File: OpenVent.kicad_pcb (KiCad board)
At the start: 2 copper layers, 195.5 x 61 mm, 217 parts, among them CN1 2x10_Way_2.54mm_Pitch_Header, J1 OpenVent_Barrel_Connector, Q1 DMMT5401-7-F, Q12 2N7002BK, Q13 2N7002BK, Q14 AOD4185, Q2 AOD4185, Q3 AOD4185, Q4 DMMT5401-7-F, Q5 2N7002BK, Q6 2N7002BK, Q7 2N7002BK, Q8 SSM3K341R, Q9 2N7002BK, U1 TMP236A4DBZT, U10 MPXV4006GP, U11 MPXV4006DP, U12 TLV2333IDR, U13 TLV7042DGKR, U14 LT3796, U15 FT2232HL-REEL, U16 TLV2333IDR, U2 STM32L412R8T6, U3 TI_TXB0108PWR, U4 BD50FC0WEFJ-E2, U5 LDL212D33R, U6 LDL212D33R, U7 LMC6772AIMX, U8 VNH5019ATR-E, U9 LDL212D33R, X1 ABM3B-16.000MHZ, X2 ABM3B-12.000MHZ

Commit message: Update OpenVent.kicad_pcb
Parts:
- JP2: moved to B.Cu
- moved JP2 50.9 mm to (142.7, 123.2), turned to 270 degrees
- moved C10 25.0 mm to (75.0, 124.4)
- moved C7 25.0 mm to (71.0, 124.4)
- moved D1 25.0 mm to (53.5, 126.9)
- moved TVS1 25.0 mm to (67.1, 125.1)
- moved C4 25.0 mm to (71.0, 126.9)
- moved FL1 25.0 mm to (74.8, 126.9)
- moved RV1 25.0 mm to (61.8, 125.9)
- moved C15 13.0 mm to (226.3, 109.4)
- moved C16 13.0 mm to (229.8, 98.6)
- moved C40 13.0 mm to (167.1, 104.1)
- moved C41 13.0 mm to (174.1, 96.8)
- moved C53 13.0 mm to (159.1, 105.2)
- moved D3 13.0 mm to (71.8, 87.2)
- moved D4 13.0 mm to (67.8, 87.2)
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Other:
- board size 195.5 x 61 mm -> 195.5 x 76.2 mm

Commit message: Mounting holes x4 have been added to the PCB
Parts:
- added C110: 1uF_0603_Ceramic_Capacitor,_10%,_50V,_X5R, Capacitor_SMD:C_0603_1608Metric, F.Cu at (400.1, 24.1)
- added C117: 1uF_0603_Ceramic_Capacitor,_10%,_50V,_X5R, Capacitor_SMD:C_0603_1608Metric, F.Cu at (396.1, 26.6)
- added C13: 1uF_0603_Ceramic_Capacitor,_10%,_50V,_X5R, Capacitor_SMD:C_0603_1608Metric, F.Cu at (415.3, 33.0)
- added C22: 10nF_0603_Ceramic_Capacitor,_10%,_50V,_X7R-, Capacitor_SMD:C_0603_1608Metric, F.Cu at (374.1, 15.8)
- added C62: 10uF_0805_Ceramic_Capacitor_10%_X7R_10V, Capacitor_SMD:C_0805_2012Metric, F.Cu at (365.5, 21.8)
- added C63: 10uF_0805_Ceramic_Capacitor_10%_X7R_10V, Capacitor_SMD:C_0805_2012Metric, F.Cu at (361.0, 21.8)
- added C64: 470pF_0603_Ceramic_Capacitor,_5%,_100V,_C0G, Capacitor_SMD:C_0603_1608Metric, F.Cu at (374.4, 13.3)
- added C65: 10uF_0805_Ceramic_Capacitor_10%_X7R_10V, Capacitor_SMD:C_0805_2012Metric, F.Cu at (356.6, 21.8)
- added C66: 100nF_0603_Ceramic_Capacitor,_10%,_X7R,_25V, Capacitor_SMD:C_0603_1608Metric, F.Cu at (375.7, 10.8)
- added C67: 10nF_0603_Ceramic_Capacitor,_10%,_50V,_X7R-, Capacitor_SMD:C_0603_1608Metric, F.Cu at (370.1, 15.8)
- added C68: 1uF_0603_Ceramic_Capacitor,_10%,_50V,_X5R, Capacitor_SMD:C_0603_1608Metric, F.Cu at (375.7, 8.25)
- added C69: 470pF_0603_Ceramic_Capacitor,_5%,_100V,_C0G, Capacitor_SMD:C_0603_1608Metric, F.Cu at (370.4, 13.3)
- added C70: 10nF_0603_Ceramic_Capacitor,_10%,_50V,_X7R-, Capacitor_SMD:C_0603_1608Metric, F.Cu at (371.7, 10.8)
- added C71: 470pF_0603_Ceramic_Capacitor,_5%,_100V,_C0G, Capacitor_SMD:C_0603_1608Metric, F.Cu at (376.3, 3.23)
- added C72: 1uF_0603_Ceramic_Capacitor,_10%,_50V,_X5R, Capacitor_SMD:C_0603_1608Metric, F.Cu at (371.7, 8.25)
- added C73: 1uF_0603_Ceramic_Capacitor,_10%,_50V,_X5R, Capacitor_SMD:C_0603_1608Metric, F.Cu at (376.3, 5.74)
- added C74: C_1206_47nF_16V_2%_PPS_film, Capacitor_SMD:C_1206_3216Metric, F.Cu at (358.2, 7.84)
- added C75: C_1206_47nF_16V_2%_PPS_film, Capacitor_SMD:C_1206_3216Metric, F.Cu at (352.5, 15.0)
- added C76: C_1206_47nF_16V_2%_PPS_film, Capacitor_SMD:C_1206_3216Metric, F.Cu at (362.8, 1.14)
- added C77: C_1206_47nF_16V_2%_PPS_film, Capacitor_SMD:C_1206_3216Metric, F.Cu at (352.5, 11.6)
- added C78: C_1206_47nF_16V_2%_PPS_film, Capacitor_SMD:C_1206_3216Metric, F.Cu at (357.1, 1.14)
- added C79: C_1206_47nF_16V_2%_PPS_film, Capacitor_SMD:C_1206_3216Metric, F.Cu at (357.1, 4.49)
- added C80: C_1206_47nF_16V_2%_PPS_film, Capacitor_SMD:C_1206_3216Metric, F.Cu at (352.5, 8.29)
- added C81: C_1206_47nF_16V_2%_PPS_film, Capacitor_SMD:C_1206_3216Metric, F.Cu at (362.8, 4.49)
- added C82: C_1206_47nF_16V_2%_PPS_film, Capacitor_SMD:C_1206_3216Metric, F.Cu at (358.2, 11.2)
- added C93: 22uF_1206_Ceramic_Capacitor,_10%,_10V,_X7R, Resistor_SMD:R_1206_3216Metric, F.Cu at (417.3, 23.6)
- added C94: 22uF_1206_Ceramic_Capacitor,_10%,_10V,_X7R, Resistor_SMD:R_1206_3216Metric, F.Cu at (417.3, 20.3)
- added D19: LED_GREEN_0603_SMD, LED_SMD:LED_0603_1608Metric, F.Cu at (385.6, 29.3)
- added J2: Conn_01x02, Connector_PinSocket_2.54mm:PinSocket_1x02_P2.54mm_Vertical, F.Cu at (352.0, 1.79)
- added J3: Conn_01x02, Connector_PinSocket_2.54mm:PinSocket_1x02_P2.54mm_Vertical, F.Cu at (412.2, 21.0)
- added J4: Conn_01x02, Connector_PinSocket_2.54mm:PinSocket_1x02_P2.54mm_Vertical, F.Cu at (407.6, 21.0)
- added JP2: Pin_Header,_1x5-Way,_2.54mm_Pitch, Connector_PinHeader_2.54mm:PinHeader_1x05_P2.54mm_Vertical, F.Cu at (386.7, 1.79)
- added JP5: Pin_Header,_1x6-Way,_2.54mm_Pitch, Connector_PinHeader_2.54mm:PinHeader_1x06_P2.54mm_Vertical, F.Cu at (352.0, 22.6)
- added R10: 100K_0603_Chip_Resistor,_1%,_0.1W, Resistor_SMD:R_0603_1608Metric, F.Cu at (407.3, 33.0)
- added R113: 0R1_0603_Chip_Resistor,_1%,_0.1W, Resistor_SMD:R_0603_1608Metric, F.Cu at (396.1, 21.6)
- added R119: 10k_0603_Chip_Resistor,_1%,_0.1W, Resistor_SMD:R_0603_1608Metric, F.Cu at (389.7, 29.3)
- added R120: 10k_0603_Chip_Resistor,_1%,_0.1W, Resistor_SMD:R_0603_1608Metric, F.Cu at (396.1, 24.1)
- added R122: 0R1_0603_Chip_Resistor,_1%,_0.1W, Resistor_SMD:R_0603_1608Metric, F.Cu at (400.1, 21.6)
- added R124: 10k_0603_Chip_Resistor,_1%,_0.1W, Resistor_SMD:R_0603_1608Metric, F.Cu at (393.7, 29.3)
- added R19: 2k4_0603_Chip_Resistor,_1%,_0.1W, Resistor_SMD:R_0603_1608Metric, F.Cu at (356.4, 24.6)
- added R20: 2k4_0603_Chip_Resistor,_1%,_0.1W, Resistor_SMD:R_0603_1608Metric, F.Cu at (360.4, 24.6)
- added R27: 18k_0603_Chip_Resistor,_1%,_0.1W, Resistor_SMD:R_0603_1608Metric, F.Cu at (366.1, 15.8)
- added R39: R_0603_47K_0.1%_0.1W_Film, Resistor_SMD:R_0603_1608Metric_Pad0.98x0.95mm_HandSolder, F.Cu at (367.8, 3.23)
- added R42: R_0603_47K_0.1%_0.1W_Film, Resistor_SMD:R_0603_1608Metric_Pad0.98x0.95mm_HandSolder, F.Cu at (372.1, 3.23)
- added R43: R_0603_47K_0.1%_0.1W_Film, Resistor_SMD:R_0603_1608Metric_Pad0.98x0.95mm_HandSolder, F.Cu at (367.8, 0.72)
- added R49: R_0603_47K_0.1%_0.1W_Film, Resistor_SMD:R_0603_1608Metric_Pad0.98x0.95mm_HandSolder, F.Cu at (363.2, 7.42)
- added R50: R_0603_47K_0.1%_0.1W_Film, Resistor_SMD:R_0603_1608Metric_Pad0.98x0.95mm_HandSolder, F.Cu at (367.5, 8.25)
- added R53: R_0603_47K_0.1%_0.1W_Film, Resistor_SMD:R_0603_1608Metric_Pad0.98x0.95mm_HandSolder, F.Cu at (376.5, 0.72)
- added R54: R_0603_47K_0.1%_0.1W_Film, Resistor_SMD:R_0603_1608Metric_Pad0.98x0.95mm_HandSolder, F.Cu at (372.1, 5.74)
- added R55: R_0603_47K_0.1%_0.1W_Film, Resistor_SMD:R_0603_1608Metric_Pad0.98x0.95mm_HandSolder, F.Cu at (367.5, 10.8)
- added R56: R_0603_47K_0.1%_0.1W_Film, Resistor_SMD:R_0603_1608Metric_Pad0.98x0.95mm_HandSolder, F.Cu at (361.9, 14.1)
- added R57: R_0603_47K_0.1%_0.1W_Film, Resistor_SMD:R_0603_1608Metric_Pad0.98x0.95mm_HandSolder, F.Cu at (366.2, 13.3)
- added R58: R_0603_47K_0.1%_0.1W_Film, Resistor_SMD:R_0603_1608Metric_Pad0.98x0.95mm_HandSolder, F.Cu at (372.1, 0.72)
- added R59: R_0603_47K_0.1%_0.1W_Film, Resistor_SMD:R_0603_1608Metric_Pad0.98x0.95mm_HandSolder, F.Cu at (367.8, 5.74)
- added R6: 10k_0603_Chip_Resistor,_1%,_0.1W, Resistor_SMD:R_0603_1608Metric, F.Cu at (411.3, 35.5)
- added R60: R_0603_47K_0.1%_0.1W_Film, Resistor_SMD:R_0603_1608Metric_Pad0.98x0.95mm_HandSolder, F.Cu at (363.2, 9.93)
- added R61: R_0603_47K_0.1%_0.1W_Film, Resistor_SMD:R_0603_1608Metric_Pad0.98x0.95mm_HandSolder, F.Cu at (357.5, 14.1)
- added R72: 12k_0603_Chip_Resistor,_1%,_0.1W, Resistor_SMD:R_0603_1608Metric, F.Cu at (418.2, 0.72)
- added R8: 100K_0603_Chip_Resistor,_1%,_0.1W, Resistor_SMD:R_0603_1608Metric, F.Cu at (411.3, 33.0)
- added R86: 12k_0603_Chip_Resistor,_1%,_0.1W, Resistor_SMD:R_0603_1608Metric, F.Cu at (407.3, 27.1)
- added R87: 12k_0603_Chip_Resistor,_1%,_0.1W, Resistor_SMD:R_0603_1608Metric, F.Cu at (411.3, 27.1)
- added R9: 1K_0603_Chip_Resistor,_1%,_0.1W, Resistor_SMD:R_0603_1608Metric, F.Cu at (407.3, 35.5)
- added REF**: MountingHole_3.2mm_M3, MountingHole:MountingHole_3.2mm_M3, F.Cu at (238.0, 118.9)
- added REF**: MountingHole_3.2mm_M3, MountingHole:MountingHole_3.2mm_M3, F.Cu at (238.0, 70.0)
- added REF**: MountingHole_3.2mm_M3, MountingHole:MountingHole_3.2mm_M3, F.Cu at (70.0, 118.9)
- added REF**: MountingHole_3.2mm_M3, MountingHole:MountingHole_3.2mm_M3, F.Cu at (70.0, 70.0)
- added U26: LDL212D33R, Package_SO:SO-8_5.3x6.2mm_P1.27mm, F.Cu at (388.8, 24.2)
- U2: value STM32L412R8T6 -> STM32L476RGLQFP64
- moved R14 163.9 mm to (329.1, -33.7)
- moved C101 163.9 mm to (325.1, -34.8)
- moved D2 163.9 mm to (319.9, -31.9)
- moved Q4 163.9 mm to (308.9, -24.8)
- moved R10 163.9 mm to (325.1, -32.3)
- moved R13 163.9 mm to (325.1, -29.8)
- moved R9 163.9 mm to (329.1, -36.2)
- moved C106 163.9 mm to (318.7, -26.4)
- moved C99 163.9 mm to (321.6, -23.9)
- moved R11 163.9 mm to (313.5, -23.2)
- moved R110 163.9 mm to (322.8, -26.4)
- moved R15 163.9 mm to (313.5, -25.7)
- moved R8 163.9 mm to (317.6, -23.9)
- moved C103 163.9 mm to (301.4, -25.1)
- moved Q1 163.9 mm to (296.8, -24.2)
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- renumbered C16 to C101, C17 to C103, C18 to C105, C19 to C106, C20 to C108, C15 to C99, R12 to R110, U4 to U22, U5 to U23, U6 to U24
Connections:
- net /JTAG/J_1V8 renamed V1V8
- net ISNS renamed Net-(U2-Pad24)
- net MOTOR-CTRL-STATUS renamed SPI1_MOSI
- net Net-(U15-Pad21) renamed /JTAG/NRST
- net Net-(U15-Pad38) renamed /JTAG/TxD_S
- net Net-(U15-Pad39) renamed /JTAG/RxD_S
- net STAT2 renamed PWR_UP
- net TCK renamed /JTAG/TCK
- net TDI renamed /JTAG/TDI
- net TDO renamed /JTAG/TDO
- net TMS renamed /JTAG/TMS
- net nALERT-ENABLE renamed Net-(U2-Pad2)
- net nPRESSURE-ALERT renamed nPRESSURE-PATIENT-ALERT
- net nSTAT1 renamed Net-(U2-Pad53)
- net nVBATT-ALERT renamed SW_HOME
- C10 pad 2: +3V3 -> VDC
- C101 pad 2: Net-(C16-Pad2) -> +5V
- C32 pad 1: FLOW-SENSOR-GAIN -> FLOW_SENS_GAIN
- C34 pad 2: OXYGEN-SENSOR -> O2_SENS
- C41 pad 1: /JTAG/J_3V3 -> +3V3
- C99 pad 2: Net-(C15-Pad2) -> +5V
- D1 pad 1: (no net) -> Net-(D1-Pad1)
- D1 pad 2: (no net) -> GND
- FB2 pad 1: /JTAG/J_3V3 -> +3V3
- FB3 pad 1: /JTAG/J_3V3 -> +3V3
- JP4 pad 4: /Microcontroller/USART-STM-RX -> Net-(JP4-Pad4)
- JP4 pad 5: /Microcontroller/USART-STM-TX -> Net-(JP4-Pad5)
- R37 pad 1: Net-(CN4-Pad1) -> FLOW_SENS_DRCT
- R4 pad 1: Net-(D1-PadA) -> Net-(D1-Pad1)
- R44 pad 2: FLOW-SENSOR-GAIN -> FLOW_SENS_GAIN
- R48 pad 2: OXYGEN-SENSOR -> O2_SENS
- R5 pad 2: +3V3 -> VDC
- R76 pad 1: /JTAG/J_3V3 -> +3V3
- TVS2 pad 6: Net-(C40-Pad1) -> Net-(TVS2-Pad6)
- U10 pad 4: Net-(C28-Pad2) -> PRES_SENS_PAT
- U11 pad 2: +5V -> Net-(R35-Pad1)
- U11 pad 4: Net-(CN4-Pad1) -> Net-(R36-Pad1)
- U12 pad 1: OXYGEN-SENSOR -> O2_SENS
- U12 pad 7: FLOW-SENSOR-GAIN -> FLOW_SENS_GAIN
- U15 pad 20: /JTAG/J_3V3 -> +3V3
- U15 pad 31: /JTAG/J_3V3 -> +3V3
- U15 pad 42: /JTAG/J_3V3 -> +3V3
- U15 pad 50: /JTAG/J_3V3 -> +3V3
- U15 pad 56: /JTAG/J_3V3 -> +3V3
- U15 pad 60: Net-(U15-Pad60) -> Net-(D11-Pad2)
- U2 pad 11: FLOW-SENSOR -> Net-(U2-Pad11)
- U2 pad 14: PRESSURE-SENSOR -> PB_SEL_MCU
- U2 pad 15: OXYGEN-SENSOR -> PWM
- U2 pad 16: Net-(U1-Pad2) -> /Microcontroller/BUZZER_PWM
- U2 pad 17: /Microcontroller/ANALOG-SPARE -> Net-(U2-Pad17)
- U2 pad 20: FLOW-SENSOR-GAIN -> SPI1_FPGA_CS
- U2 pad 21: PWM -> SPI1_SCLK
- U2 pad 22: /Microcontroller/ENC-1 -> SPI1_MISO
- U2 pad 26: Net-(U2-Pad26) -> FAN_DRIVE
- U2 pad 27: Net-(U2-Pad27) -> FPGA_READY
- U2 pad 29: /Microcontroller/SW-3 -> Net-(U2-Pad29)
- U2 pad 30: /Microcontroller/SW-4 -> Net-(U2-Pad30)
- U2 pad 38: LDO-EN -> ON
- U2 pad 39: nVDC-ALERT -> SW_END
- U2 pad 41: /Microcontroller/ENC-2 -> SW_BACKUP
- U2 pad 42: /Microcontroller/USART-STM-TX -> TxD_M
- U2 pad 43: /Microcontroller/USART-STM-RX -> RxD_M
- U2 pad 46: /Microcontroller/SWD-DIO -> TMS_M
- U2 pad 48: VDC -> +3V3
- U2 pad 49: /Microcontroller/SWD-CLK -> TCK_M
- U2 pad 50: /Microcontroller/LIMIT-2 -> TDI_M
- U2 pad 54: /Microcontroller/LIMIT-1 -> Net-(U2-Pad54)
- U2 pad 55: Net-(U2-Pad55) -> TDO_M
- U2 pad 61: /Microcontroller/SW-1 -> VIN_FAIL_M
- U2 pad 62: /Microcontroller/SW-2 -> Net-(U2-Pad62)
- U2 pad 7: /Microcontroller/~RESET~ -> NRST_M
- U2 pad 8: SOUNDER-CURRENT -> Net-(U2-Pad8)
- U22 pad 8: Net-(C15-Pad2) -> +5V
- U24 pad 4: Net-(C16-Pad2) -> +5V
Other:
- copper layers 2 -> 4

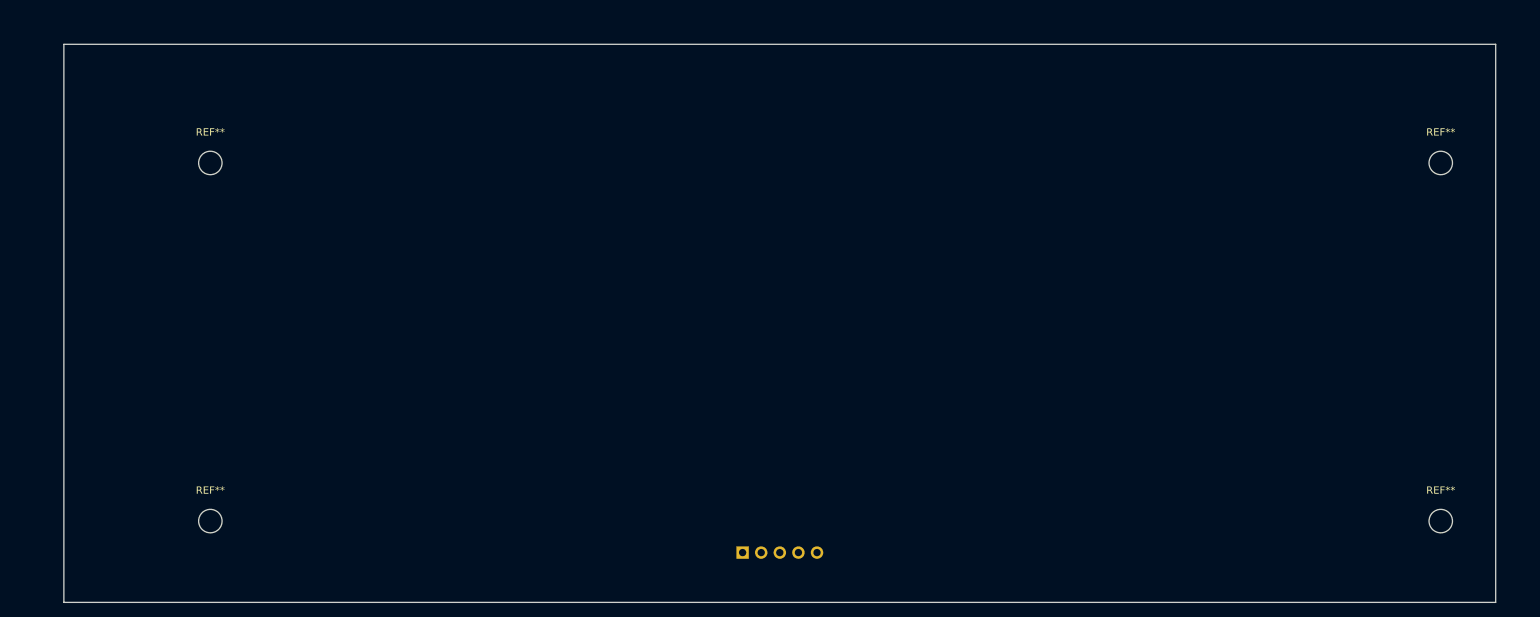
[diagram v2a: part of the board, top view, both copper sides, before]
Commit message: Update OpenVent.kicad_pcb
Updated the PCB dimension/edge layer with reference to the PCBs dimension diagram.
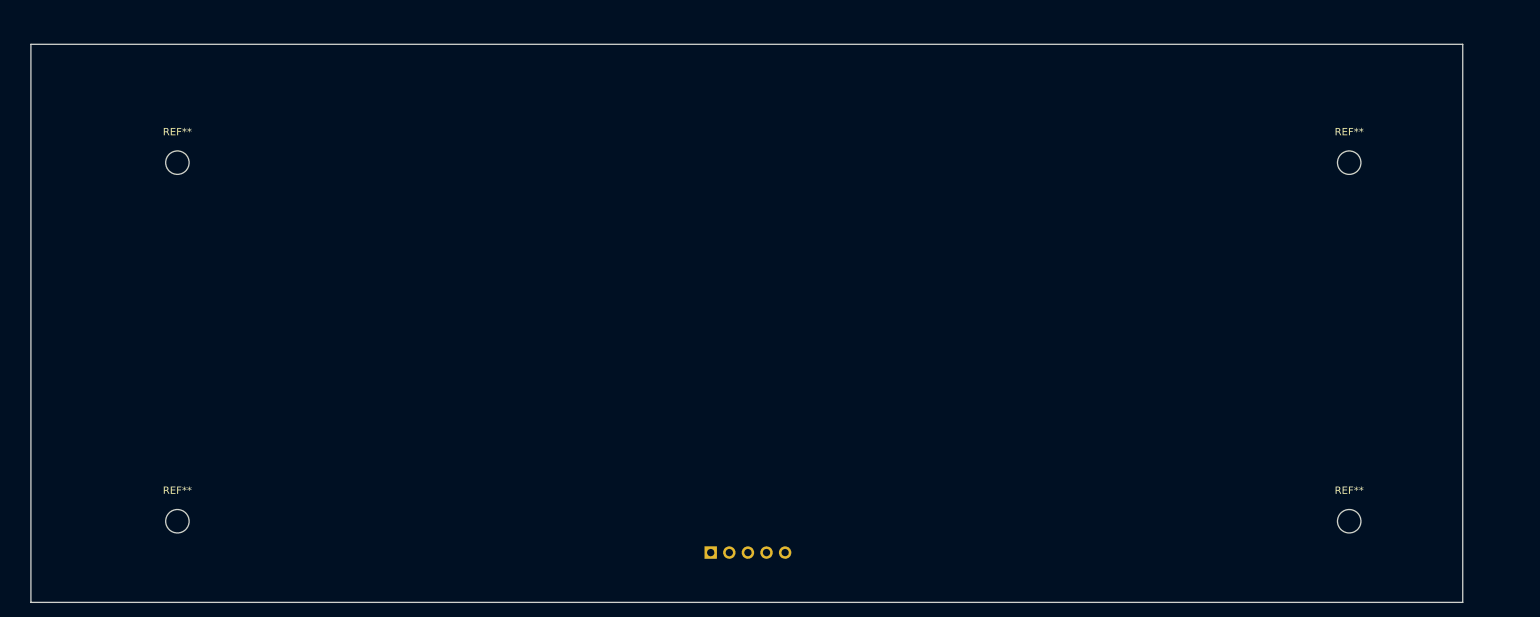
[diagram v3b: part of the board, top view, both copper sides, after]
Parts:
- moved REF** 12.5 mm to (225.5, 70.0)
- moved REF** 12.5 mm to (225.5, 118.9)
- moved REF** 4.50 mm to (65.5, 70.0)
- moved REF** 4.50 mm to (65.5, 118.9)
- moved JP2 4.36 mm to (138.3, 123.2)

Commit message: Update OpenVent.kicad_pcb
Organized some components together
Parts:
- added C102: 2.2uF_0603_Ceramic_Capacitor,_10%,_50V,_X5R, Capacitor_SMD:C_0603_1608Metric, F.Cu at (411.9, 94.8)
- added C122: 100nF_0603_Ceramic_Capacitor,_10%,_X7R,_25V, Capacitor_SMD:C_0603_1608Metric, F.Cu at (380.1, 113.8)
- added C123: 2.2uF_0603_Ceramic_Capacitor,_10%,_50V,_X5R, Capacitor_SMD:C_0603_1608Metric, F.Cu at (409.6, 98.5)
- added C124: 1uF_0603_Ceramic_Capacitor,_10%,_50V,_X5R, Capacitor_SMD:C_0603_1608Metric, F.Cu at (381.5, 101.9)
- added FB4: BLM18AG601SN1D Chip_Ferrite,_600R,_0603,_750mA, Capacitor_SMD:C_0603_1608Metric, F.Cu at (401.8, 96.0)
- added R12: 1K_0603_Chip_Resistor,_1%,_0.1W, Resistor_SMD:R_0603_1608Metric, F.Cu at (409.6, 106.1)
- added R127: 100K_0603_Chip_Resistor,_1%,_0.1W, Resistor_SMD:R_0603_1608Metric, F.Cu at (384.1, 113.8)
- added R135: 0R1_0603_Chip_Resistor,_1%,_0.1W, Resistor_SMD:R_0603_1608Metric, F.Cu at (413.6, 98.5)
- added R136: 0R1_0603_Chip_Resistor,_1%,_0.1W, Resistor_SMD:R_0603_1608Metric, F.Cu at (379.2, 98.0)
- added U17: MPXV4006GP, OpenVent:NXP-CASE-1369_482C, F.Cu at (434.6, 121.2)
- C101, C117: value 1uF_0603_Ceramic_Capacitor,_10%,_50V,_X5R -> 2.2uF_0603_Ceramic_Capacitor,_10%,_50V,_X5R
- C13: value 100nF_0603_Ceramic_Capacitor,_10%,_X7R,_25V -> 1uF_0603_Ceramic_Capacitor,_10%,_50V,_X5R
- C22: value 1000uF_25V_Aluminium_SMD_Capacitor,_20% -> 10nF_0603_Ceramic_Capacitor,_10%,_50V,_X7R-; footprint Capacitor_SMD:CP_Elec_10x10 -> Capacitor_SMD:C_0603_1608Metric
- CN1: value 2x10_Way_2.54mm_Pitch_Header -> 2x5_Way_1.27mm_Pitch_Header_MCU; footprint Connector_PinHeader_2.54mm:PinHeader_2x10_P2.54mm_Vertical -> Connector_PinSocket_1.27mm:PinSocket_2x04_P1.27mm_Horizontal
- D12, D14: value BB-HRGB32M-TRB -> LED_GREEN_0603_SMD; footprint OpenVent:LED_RGB_BL-RRGB32M_TRB_PLCC4_3.2x2.8mm -> LED_SMD:LED_0603_1608Metric
- D13: value BB-HRGB32M-TRB -> LED_Red_0603_SMD; footprint OpenVent:LED_RGB_BL-RRGB32M_TRB_PLCC4_3.2x2.8mm -> LED_SMD:LED_0603_1608Metric
- D2: value FSV20100V -> LED_GREEN_0603_SMD; footprint Package_TO_SOT_SMD:TO-277A -> LED_SMD:LED_0603_1608Metric
- JP3: value Pin_Header,_1x6-Way,_2.54mm_Pitch -> Pin_Header,_1x6-Way,_2.54mm_Pitch, Mpn 640456-6; footprint Connector_PinHeader_2.54mm:PinHeader_1x06_P2.54mm_Vertical -> Connector_PinHeader_2.54mm:PinHeader_1x06_P2.54mm_Horizontal
- R1: value 10k_0603_Chip_Resistor,_1%,_0.1W -> R_0603_2k74_0.1W_0.1%
- R10, R8: value 1M_0603_Chip_Resistor,_1%,_0.1W -> 100K_0603_Chip_Resistor,_1%,_0.1W
- R11, R28, R9: value 1M_0603_Chip_Resistor,_1%,_0.1W -> 1K_0603_Chip_Resistor,_1%,_0.1W
- R19, R20: value 1K_0603_Chip_Resistor,_1%,_0.1W -> 2k4_0603_Chip_Resistor,_1%,_0.1W
- R2: value 20k_0603_Chip_Resistor,_1%,_0.1W -> R_0603_2k74_0.1W_0.1%
- R26: value 0.025 Ohm 1W 1% -> 1K_0603_Chip_Resistor,_1%,_0.1W; footprint Resistor_SMD:R_2010_5025Metric -> Resistor_SMD:R_0603_1608Metric
- R27: value 10k_0603_Chip_Resistor,_1%,_0.1W -> 18k_0603_Chip_Resistor,_1%,_0.1W
- R3: value DNF_0603 -> R_0603_2k74_0.1W_0.1%
- R38, R39, R54: value 100K_0603_Chip_Resistor,_1%,_0.1W -> R_0603_47K_0.1%_0.1W_Film; footprint Resistor_SMD:R_0603_1608Metric -> Resistor_SMD:R_0603_1608Metric_Pad0.98x0.95mm_HandSolder
- R42, R43: value 200k_0603_Chip_Resistor,_0.1%,_0.1W -> R_0603_47K_0.1%_0.1W_Film; footprint Resistor_SMD:R_0603_1608Metric -> Resistor_SMD:R_0603_1608Metric_Pad0.98x0.95mm_HandSolder
- R49, R55: value 20k_0603_Chip_Resistor,_1%,_0.1W -> R_0603_47K_0.1%_0.1W_Film; footprint Resistor_SMD:R_0603_1608Metric -> Resistor_SMD:R_0603_1608Metric_Pad0.98x0.95mm_HandSolder
- R50: value 10k_0603_Chip_Resistor,_1%,_0.1W -> R_0603_47K_0.1%_0.1W_Film; footprint Resistor_SMD:R_0603_1608Metric -> Resistor_SMD:R_0603_1608Metric_Pad0.98x0.95mm_HandSolder
- R53: value R_0603_806K_0.1W_1% -> R_0603_47K_0.1%_0.1W_Film; footprint Resistor_SMD:R_0603_1608Metric -> Resistor_SMD:R_0603_1608Metric_Pad0.98x0.95mm_HandSolder
- R56: value R_0603_499R_0.1W_1% -> R_0603_47K_0.1%_0.1W_Film; footprint Resistor_SMD:R_0603_1608Metric -> Resistor_SMD:R_0603_1608Metric_Pad0.98x0.95mm_HandSolder
- R57: value R_0603_40k2K_0.1W_1% -> R_0603_47K_0.1%_0.1W_Film; footprint Resistor_SMD:R_0603_1608Metric -> Resistor_SMD:R_0603_1608Metric_Pad0.98x0.95mm_HandSolder
- R58: value R_0603_19k6_0.1W_1% -> R_0603_47K_0.1%_0.1W_Film; footprint Resistor_SMD:R_0603_1608Metric -> Resistor_SMD:R_0603_1608Metric_Pad0.98x0.95mm_HandSolder
- R59: value R_0603_499K_0.1W_1% -> R_0603_47K_0.1%_0.1W_Film; footprint Resistor_SMD:R_0603_1608Metric -> Resistor_SMD:R_0603_1608Metric_Pad0.98x0.95mm_HandSolder
- R60: value R_0603_97.6K_0.1W_1% -> R_0603_47K_0.1%_0.1W_Film; footprint Resistor_SMD:R_0603_1608Metric -> Resistor_SMD:R_0603_1608Metric_Pad0.98x0.95mm_HandSolder
- R61: value R_0603_2k_0.1W_1% -> R_0603_47K_0.1%_0.1W_Film; footprint Resistor_SMD:R_0603_1608Metric -> Resistor_SMD:R_0603_1608Metric_Pad0.98x0.95mm_HandSolder
- R72: value 1K_0603_Chip_Resistor,_1%,_0.1W -> 12k_0603_Chip_Resistor,_1%,_0.1W
- U24: value LDL212D33R -> BD50FC0WEFJ-E2; footprint Package_SO:SO-8_5.3x6.2mm_P1.27mm -> Package_SO:HSOP-8-1EP_3.9x4.9mm_P1.27mm_EP2.41x3.1mm_ThermalVias
- moved Q14 208.1 mm to (237.5, -75.9)
- moved R120 198.9 mm to (228.6, -83.3)
- moved R119 198.7 mm to (223.5, -79.7)
- moved D2 196.1 mm to (127.2, -68.0)
- moved Q9 181.9 mm to (114.2, -69.0)
- moved U24 152.3 mm to (388.3, 100.7)
- moved D16 145.9 mm to (344.5, 92.6)
- moved C101 145.3 mm to (464.7, 5.50)
- moved Q12 141.3 mm to (108.3, -64.3)
- moved R13 138.5 mm to (459.4, 4.20)
- moved Q13 137.3 mm to (226.8, -77.1)
- moved Q8 136.2 mm to (118.7, -63.1)
- moved R110 132.4 mm to (310.5, 105.4)
- moved R14 131.4 mm to (363.2, 93.2)
- moved C103 131.0 mm to (350.5, 96.3), turned to 270 degrees
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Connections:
- net /Microcontroller/SWD-DIO renamed Net-(CN1-Pad7)
- C101 pad 1: GND -> +5V
- C101 pad 2: +5V -> GND
- C117 pad 1: +3.3V -> +3V3
- C13 pad 2: +5V -> Net-(C13-Pad2)
- C22 pad 1: (no net) -> GND
- C22 pad 2: (no net) -> +5V
- C93 pad 1: +5V -> Net-(C87-Pad1)
- C94 pad 1: +5V -> Net-(C88-Pad1)
- CN1 pad 2: Net-(CN1-Pad2) -> TMS_M
- CN1 pad 3: Net-(CN1-Pad3) -> GND
- CN1 pad 4: GND -> TCK_M
- CN1 pad 5: Net-(CN1-Pad5) -> GND
- CN1 pad 6: GND -> TDO_M
- CN1 pad 8: GND -> TDI_M
- D12 pad 1: +5V -> Net-(D12-Pad1)
- D12 pad 2: Net-(D12-Pad2) -> GND
- D13 pad 1: +5V -> Net-(D13-Pad1)
- D13 pad 2: Net-(D13-Pad2) -> /JTAG/DONE
- D14 pad 1: +5V -> Net-(D14-Pad1)
- D14 pad 2: Net-(D14-Pad2) -> GND
- D2 pad 1: Net-(D2-Pad1) -> VDC
- D2 pad 2: Net-(D2-Pad1) -> Net-(D2-Pad2)
- JP2 pad 2: /Microcontroller/SW-1 -> Net-(JP2-Pad2)
- JP2 pad 3: /Microcontroller/SW-2 -> Net-(JP2-Pad3)
- JP2 pad 4: /Microcontroller/SW-3 -> Net-(JP2-Pad4)
- JP2 pad 5: /Microcontroller/SW-4 -> Net-(JP2-Pad5)
- JP3 pad 1: +3V3 -> SPI1_SCLK
- JP3 pad 2: /Microcontroller/ENC-1 -> SPI1_MOSI
- JP3 pad 3: /Microcontroller/ENC-2 -> SPI1_MISO
- JP3 pad 4: /Microcontroller/LIMIT-1 -> SPI1_FPGA_CS
- JP3 pad 5: /Microcontroller/LIMIT-2 -> GND
- JP3 pad 6: GND -> +3V3
- R1 pad 1: Net-(FB1-Pad1) -> +5V
- R1 pad 2: +5V -> Net-(Q16-Pad2)
- R10 pad 1: GND -> Net-(R10-Pad1)
- R10 pad 2: Net-(Q2-Pad1) -> GND
- R11 pad 2: Net-(Q1-Pad4) -> Net-(R11-Pad2)
- R13 pad 1: Net-(R13-Pad1) -> Net-(IC4-Pad3)
- R19 pad 1: GND -> I2C_SDA
- R19 pad 2: PWM -> +3V3
- R2 pad 1: GND -> Net-(Q16-Pad2)
- R2 pad 2: Net-(FB1-Pad1) -> GND
- R20 pad 1: MOTOR-IN-A -> I2C_SCL
- R20 pad 2: Net-(R20-Pad2) -> +3V3
- R26 pad 1: GND -> Net-(IC1-Pad6)
- R26 pad 2: Net-(R16-Pad2) -> PB_SEL_FPGA
- R27 pad 1: ShutDown_n -> GND
- R27 pad 2: Net-(Q5-Pad1) -> Net-(R27-Pad2)
- R28 pad 1: Net-(Q5-Pad1) -> Net-(IC1-Pad4)
- R28 pad 2: +3V3 -> PB_SEL_MCU
- R3 pad 1: Net-(FB1-Pad1) -> +5V
- R3 pad 2: VDC -> Net-(Q16-Pad2)
- R38 pad 2: FLOW-SENSOR -> AD_VREF
- R39 pad 1: Net-(C28-Pad2) -> Vcap_PRES_SENS_VENT
- R39 pad 2: PRESSURE-SENSOR -> Net-(R39-Pad2)
- R42 pad 1: GND -> Vcap_PRES_SENS_PAT
- R42 pad 2: FLOW-SENSOR -> Net-(R42-Pad2)
- R43 pad 1: GND -> Vcap_FLOW_SENS_DRCT
- R43 pad 2: PRESSURE-SENSOR -> Net-(R43-Pad2)
- R49 pad 1: VIN -> Vcap_FLOW_SENS_GAIN
- R50 pad 1: Net-(R49-Pad2) -> Vcap_O2_SENS
- R50 pad 2: GND -> Net-(R50-Pad2)
- R53 pad 1: VIN -> Vcap_F
- R54 pad 1: +3V3 -> Vcap_G
- R54 pad 2: nVDC-ALERT -> Net-(R54-Pad2)
- R55 pad 1: Net-(R53-Pad2) -> PRES_SENS_VENT
- R55 pad 2: GND -> Vcap_PRES_SENS_VENT
- R56 pad 1: Net-(R56-Pad1) -> PRES_SENS_PAT
- R56 pad 2: Net-(C56-Pad1) -> Vcap_PRES_SENS_PAT
- R57 pad 1: Net-(C37-Pad1) -> FLOW_SENS_DRCT
- R57 pad 2: GND -> Vcap_FLOW_SENS_DRCT
- R58 pad 1: Net-(R58-Pad1) -> FLOW_SENS_GAIN
- R58 pad 2: GND -> Vcap_FLOW_SENS_GAIN
- R59 pad 1: VIN -> O2_SENS
- R59 pad 2: Net-(R59-Pad2) -> Vcap_O2_SENS
- R6 pad 1: /Microcontroller/~RESET~ -> NRST_M
- R6 pad 2: +3V3 -> VDC
- R60 pad 1: Net-(R59-Pad2) -> SensorOut_F
- R60 pad 2: GND -> Vcap_F
- R61 pad 1: VIN -> SensorOut_G
- R61 pad 2: Net-(R61-Pad2) -> Vcap_G
- R8 pad 1: GND -> /Microcontroller/BUZZER_PWM
- R8 pad 2: Net-(Q4-Pad1) -> GND
- R9 pad 1: GND -> Net-(C13-Pad2)
- R9 pad 2: Net-(Q1-Pad1) -> Net-(R10-Pad1)
- U2 pad 17: Net-(U2-Pad17) -> /Microcontroller/ANALOG-SPARE
- U2 pad 48: +3V3 -> VDC
- U24 pad 1: Net-(R13-Pad1) -> Net-(R136-Pad1)
- U24 pad 2: GND -> (no net)
- U24 pad 4: +5V -> (no net)
- U24 pad 6: GND -> (no net)
- U24 pad 7: GND -> (no net)
- U24 pad 8: Net-(R13-Pad1) -> +5V
